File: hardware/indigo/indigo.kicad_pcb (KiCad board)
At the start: 4 copper layers, 70.7 x 53.3 mm, 7 parts, among them J1 NEIGHBOR1, J2 NEIGHBOR2, J7 BONUS_ROW

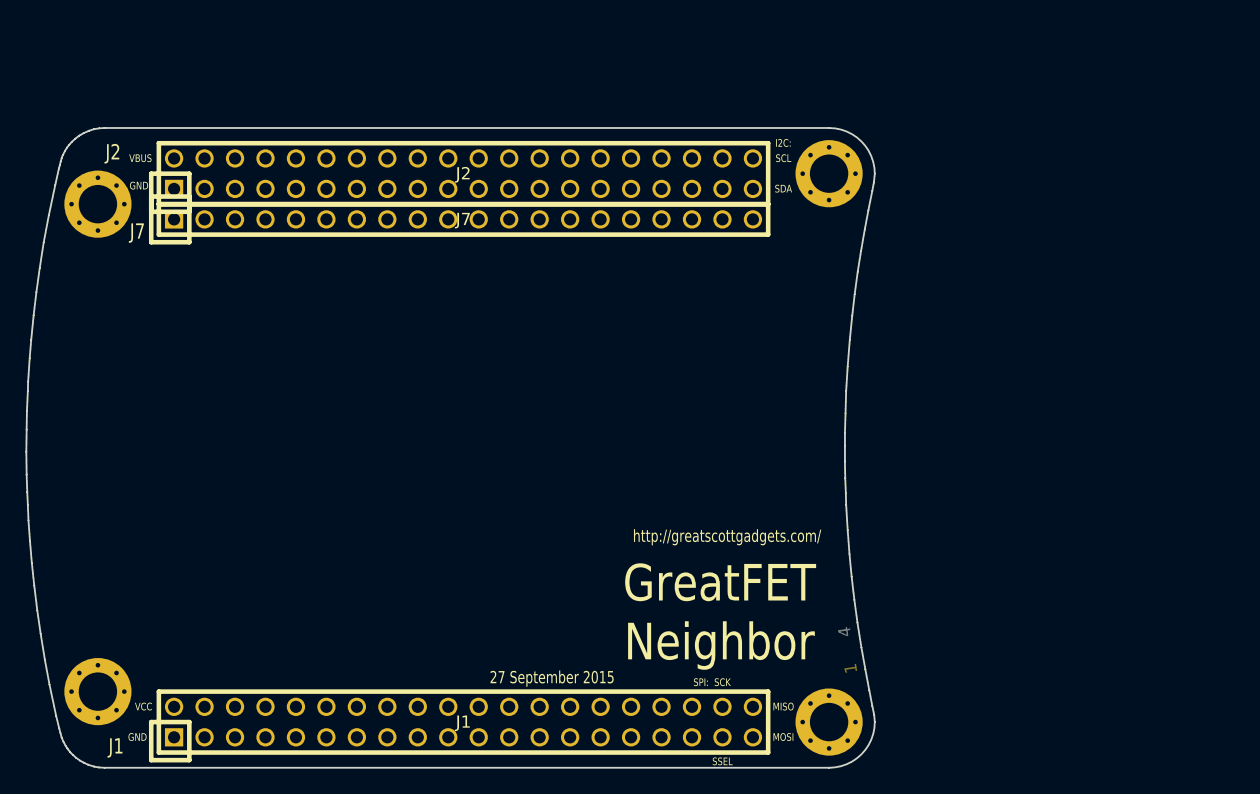
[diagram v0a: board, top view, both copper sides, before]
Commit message: Mapped connectors and did initial routing for Indigo
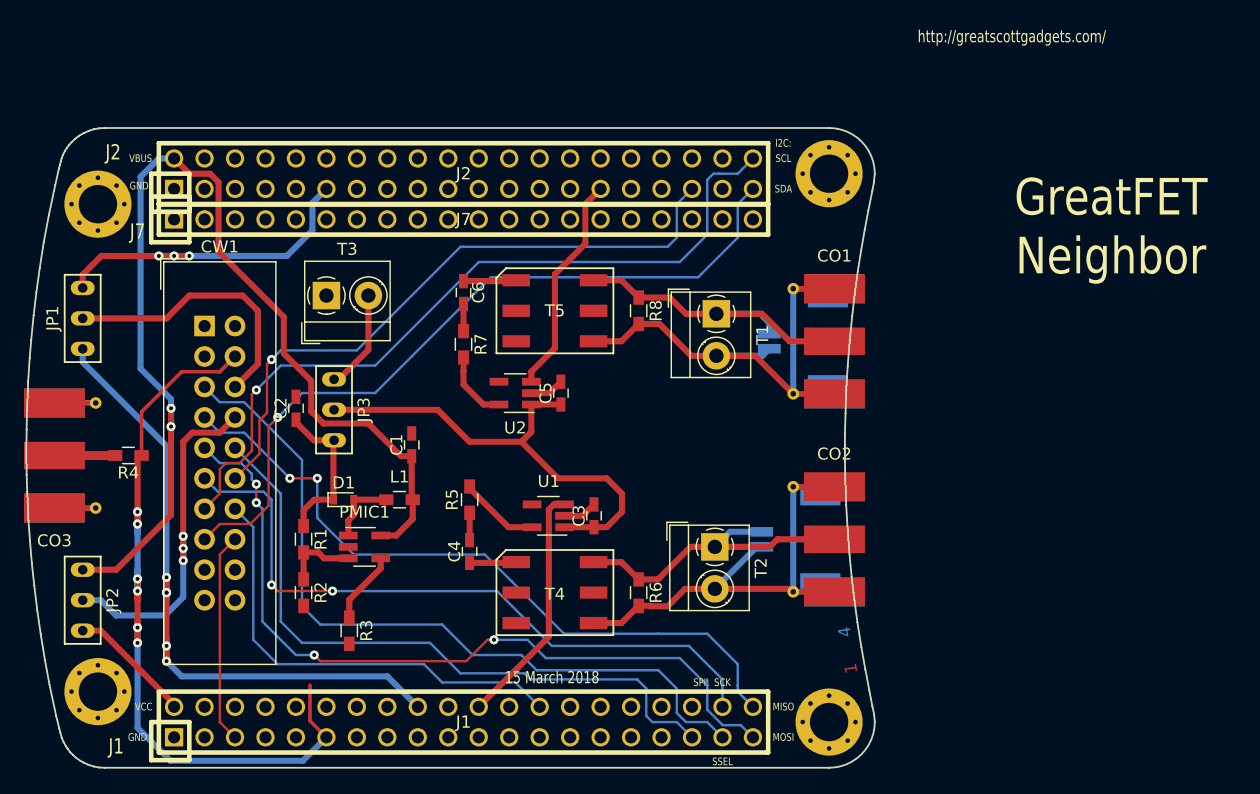
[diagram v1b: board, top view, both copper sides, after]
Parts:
- added C1: C, Capacitors_SMD:C_0603_HandSoldering, F.Cu at (141.7, 95.0)
- added C2: C, Capacitors_SMD:C_0603_HandSoldering, F.Cu at (132.1, 91.9)
- added C3: C, Capacitors_SMD:C_0603_HandSoldering, F.Cu at (156.9, 100.9)
- added C4: C, Capacitors_SMD:C_0603_HandSoldering, F.Cu at (146.6, 103.9)
- added C5: C, Capacitors_SMD:C_0603_HandSoldering, F.Cu at (154.2, 90.7)
- added C6: C, Capacitors_SMD:C_0603_HandSoldering, F.Cu at (146.1, 82.3)
- added CO1: Conn_Coaxial, Connectors_Molex:Molex_SMA_Jack_Edge_Mount, F.Cu at (175.3, 86.4)
- added CO2: Conn_Coaxial, Connectors_Molex:Molex_SMA_Jack_Edge_Mount, F.Cu at (175.3, 102.9)
- added CO3: Conn_Coaxial, Connectors_Molex:Molex_SMA_Jack_Edge_Mount, F.Cu at (113.7, 95.9)
- added CW1: CW-HEADER, Connectors_IDC:IDC-Header_2x10_Pitch2.54mm_Straight, F.Cu at (124.5, 85.1)
- added D1: D, Diodes_SMD:D_0603, F.Cu at (136.1, 99.6)
- added FF1: Conn_01x02, Connectors_Molex:Molex_Panelmate-53780-0270_02x1.25mm_Angled, B.Cu at (173.4, 102.9)
- added FF2: Conn_01x02, Connectors_Molex:Molex_Panelmate-53780-0270_02x1.25mm_Angled, B.Cu at (174.0, 86.4)
- added JP1: Jumper_NC_Dual, Indigo:JUMP3, F.Cu at (114.3, 84.5)
- added JP2: Jumper_NC_Dual, Indigo:JUMP3, F.Cu at (114.3, 108.0)
- added JP3: Jumper_NC_Dual, Indigo:JUMP3, F.Cu at (135.3, 92.1)
- added L1: L, Inductors_SMD:L_0603_HandSoldering, F.Cu at (140.7, 99.6)
- added PMIC1: AP3012, TO_SOT_Packages_SMD:SOT-23-5_HandSoldering, F.Cu at (137.8, 103.5)
- added R1: R, Resistors_SMD:R_0603_HandSoldering, F.Cu at (132.7, 102.9)
- added R2: R, Resistors_SMD:R_0603_HandSoldering, F.Cu at (132.7, 107.3)
- added R3: R, Resistors_SMD:R_0603_HandSoldering, F.Cu at (136.5, 110.5)
- added R4: 50R, Resistors_SMD:R_0603_HandSoldering, F.Cu at (118.1, 95.9)
- added R5: R-SHORTED, Resistors_SMD:R_0603_HandSoldering, F.Cu at (146.6, 99.6)
- added R6: R, Resistors_SMD:R_0603_HandSoldering, F.Cu at (160.7, 107.3)
- added R7: R-SHORTED, Resistors_SMD:R_0603_HandSoldering, F.Cu at (146.1, 86.6)
- added R8: R, Resistors_SMD:R_0603_HandSoldering, F.Cu at (160.7, 83.8)
- added T1: Screw_Terminal_01x02, TerminalBlock_MetzConnect:TerminalBlock_MetzConnect_Type059_RT06302HBWC_Pitch3.50mm, F.Cu at (167.1, 84.1)
- added T2: Screw_Terminal_01x02, TerminalBlock_MetzConnect:TerminalBlock_MetzConnect_Type059_RT06302HBWC_Pitch3.50mm, F.Cu at (167.0, 103.5)
- added T3: Screw_Terminal_01x02, TerminalBlock_MetzConnect:TerminalBlock_MetzConnect_Type059_RT06302HBWC_Pitch3.50mm, F.Cu at (134.6, 82.5)
- added T4: BALUN, Indigo:BALUN, F.Cu at (153.7, 107.3)
- added T5: BALUN, Indigo:BALUN, F.Cu at (153.7, 83.8)
- added U1: UCC2751X-SOT23-5, TO_SOT_Packages_SMD:SOT-23-5_HandSoldering, F.Cu at (153.1, 100.9)
- added U2: UCC2751X-SOT23-5, TO_SOT_Packages_SMD:SOT-23-5_HandSoldering, F.Cu at (150.4, 90.7)
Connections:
- J1 pad 10: (no net) -> /P1_1
- J1 pad 11: (no net) -> /CW_CLKIN
- J1 pad 12: (no net) -> /P1_2
- J1 pad 13: (no net) -> /P1_5
- J1 pad 14: (no net) -> /P5_2
- J1 pad 15: (no net) -> /P1_7
- J1 pad 16: (no net) -> /P1_6
- J1 pad 17: (no net) -> /P1_9
- J1 pad 18: (no net) -> /GLITCH_GEN
- J1 pad 19: (no net) -> /P5_3
- J1 pad 20: (no net) -> /P1_10
- J1 pad 21: (no net) -> /P1_12
- J1 pad 22: (no net) -> /GATE_DRIVE_SEQ1
- J1 pad 23: (no net) -> /P5_5
- J1 pad 24: (no net) -> /P5_4
- J1 pad 25: (no net) -> /P1_14
- J1 pad 26: (no net) -> /GF_GPIO1
- J1 pad 27: (no net) -> /P5_6
- J1 pad 28: (no net) -> /P1_15
- J1 pad 29: (no net) -> /P5_7
- J1 pad 3: (no net) -> /P4_9
- J1 pad 30: (no net) -> /P1_16
- J1 pad 31: (no net) -> /P1_18
- J1 pad 32: (no net) -> /P1_17
- J1 pad 33: (no net) -> /P9_5
- J1 pad 34: (no net) -> /P9_6
- J1 pad 35: (no net) -> /GF_UART_TX
- J1 pad 36: (no net) -> /P6_0
- J1 pad 37: (no net) -> /GF_SSEL
- J1 pad 38: (no net) -> /GF_SCK
- J1 pad 39: (no net) -> /GF_MOSI
- J1 pad 4: (no net) -> /P0_0
- J1 pad 40: (no net) -> /GF_MISO
- J1 pad 5: (no net) -> /CW_TRIGGER
- J1 pad 6: (no net) -> /P0_1
- J1 pad 7: (no net) -> /P1_0
- J1 pad 8: (no net) -> /P5_0
- J1 pad 9: (no net) -> /P5_1
- J2 pad 10: (no net) -> /P4_6
- J2 pad 11: (no net) -> /GF_CLKIN
- J2 pad 12: (no net) -> /CLK2
- J2 pad 13: (no net) -> /P2_8
- J2 pad 14: (no net) -> /P2_7
- J2 pad 15: (no net) -> /P2_6
- J2 pad 16: (no net) -> /P7_7
- J2 pad 17: (no net) -> /WAKEUP0
- J2 pad 18: (no net) -> /P2_5
- J2 pad 19: (no net) -> /P2_4
- J2 pad 2: /VBUS -> VBUS
- J2 pad 20: (no net) -> /P2_3
- J2 pad 21: (no net) -> /PF_4
- J2 pad 22: (no net) -> /P3_2
- J2 pad 23: (no net) -> /P7_2
- J2 pad 24: (no net) -> /P3_1
- J2 pad 25: (no net) -> /P7_1
- J2 pad 26: (no net) -> /P3_0
- J2 pad 27: (no net) -> /P7_0
- J2 pad 28: (no net) -> /P3_4
- J2 pad 29: (no net) -> /GATE_DRIVE_SEQ2
- J2 pad 3: (no net) -> /P4_8
- J2 pad 30: (no net) -> /P3_7
- J2 pad 31: (no net) -> /P6_7
- J2 pad 32: (no net) -> /P3_3
- J2 pad 33: (no net) -> /P2_2
- J2 pad 34: (no net) -> /P6_6
- J2 pad 35: (no net) -> /GF_UART_RX
- J2 pad 36: (no net) -> /P6_3
- J2 pad 37: (no net) -> /P3_5
- J2 pad 38: (no net) -> /P3_6
- J2 pad 39: (no net) -> /GF_I2C_DAT
- J2 pad 4: (no net) -> /P4_0
- J2 pad 40: (no net) -> /GF_I2C_CLK
- J2 pad 5: (no net) -> /ADC0_0
- J2 pad 6: (no net) -> /P4_5
- J2 pad 7: (no net) -> /P4_4
- J2 pad 8: (no net) -> /P4_2
- J2 pad 9: (no net) -> /P4_3
- J7 pad 11: (no net) -> /RESET
- J7 pad 12: (no net) -> /VBAT
- J7 pad 13: (no net) -> /P2_11
- J7 pad 14: (no net) -> /P2_10
- J7 pad 15: (no net) -> /P6_10
- J7 pad 16: (no net) -> /P6_9
- J7 pad 17: (no net) -> /P6_2
- J7 pad 18: (no net) -> /P6_1
- J7 pad 2: (no net) -> /P6_4
- J7 pad 3: (no net) -> /P6_5
- J7 pad 4: (no net) -> /ADC0_5
- J7 pad 5: (no net) -> /ADC0_2
- J7 pad 6: (no net) -> /P2_9
- J7 pad 7: (no net) -> /P2_12
- J7 pad 8: (no net) -> /P2_13
- J7 pad 9: (no net) -> /RTC_ALARM
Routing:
- net VBUS: track 0.00 -> 90.0 mm, vias 0 -> 2
- net /CW_CLKIN: track 0.00 -> 65.9 mm, vias 0 -> 6
- net /GF_MOSI: track 0.00 -> 65.6 mm, vias 0 -> 4
- net /Glitch Driver/DRIVE-: track 0.00 -> 65.2 mm
- net /GF_I2C_CLK: track 0.00 -> 64.4 mm, vias 0 -> 1
- net /GF_SSEL: track 0.00 -> 63.6 mm
- net /GF_I2C_DAT: track 0.00 -> 63.3 mm, vias 0 -> 1
- net /GF_MISO: track 0.00 -> 59.0 mm, vias 0 -> 2
- net /GF_SCK: track 0.00 -> 56.6 mm, vias 0 -> 2
- net /GF_UART_TX: track 0.00 -> 55.7 mm
- net /GLITCH_GEN: track 0.00 -> 55.3 mm, vias 0 -> 5
- net /Glitch Driver/DRIVE+: track 0.00 -> 54.3 mm
- net /GF_UART_RX: track 0.00 -> 53.7 mm, vias 0 -> 1
- net /Glitch Driver/V_GATEDRIVE: track 0.00 -> 39.6 mm
- net /GF_GPIO1: track 0.00 -> 38.3 mm
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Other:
- board text added: "15 March 2018"
- board text removed: "27 September 2015"
